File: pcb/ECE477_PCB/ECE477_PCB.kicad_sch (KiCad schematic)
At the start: 88 parts, among them J1 DEBUG, J10 ToF 5, J11 Pi Zero, J2 USB_B_Micro, J3 ESC, J4 ELRS, J5 AUX_PWR, J6 ToF 1, J7 ToF 2, J8 ToF 3, J9 ToF 4, M1 Brushed_DC, M2 Brushed_DC, M3 Brushed_DC, M4 Brushed_DC, Q1 IRLML6244TR, Q2 IRLML6244TR, Q3 IRLML6244TR, Q4 IRLML6244TR, SW1 RESET, U1 STM32F446RETx, U2 Pololu_S13V10F5, U3 REG1117-3.3, U4 FT230XQ, Y1 16MHz X322516MLB4SI

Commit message: completed first rev of PCB. looks like the Pi connector needs moved slightly, board radius is off but drill positions are still the same
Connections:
- net SPI1_CS: now reaches U1.20 (PA4)
- net SPI1_CS2: now reaches U1.24 (PC4)
- no-connect marks 32 -> 31
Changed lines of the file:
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@@
   (no_connect (at 193.04 38.1))
   (no_connect (at 245.11 83.82))
-  (no_connect (at 208.28 132.08))
   (no_connect (at 208.28 121.92))
   (no_connect (at 208.28 116.84))
@@
     (stroke (width 0) (type default) (color 0 0 0 0))
   )
+  (wire (pts (xy 243.84 91.44) (xy 245.11 91.44))
+    (stroke (width 0) (type default) (color 0 0 0 0))
+  )
   (wire (pts (xy 170.18 106.68) (xy 175.26 106.68))
     (stroke (width 0) (type default) (color 0 0 0 0))
@@
     (stroke (width 0) (type default) (color 0 0 0 0))
   )
+  (wire (pts (xy 205.105 132.08) (xy 208.28 132.08))
+    (stroke (width 0) (type default) (color 0 0 0 0))
+  )
   (wire (pts (xy 234.95 59.69) (xy 234.95 60.96))
     (stroke (width 0) (type default) (color 0 0 0 0))
@@
     )
   )
+  (global_label "SPI1_CS2" (shape input) (at 205.105 132.08 180) (fields_autoplaced)
+    (effects (font (size 1.27 1.27)) (justify right))
+    (property "Intersheet References" "${INTERSHEET_REFS}" (id 0) (at 193.8303 132.0006 0)
+      (effects (font (size 1.27 1.27)) (justify right) hide)
+    )
+  )
   (global_label "SPI2_MOSI" (shape input) (at 207.01 124.46 180) (fields_autoplaced)
     (effects (font (size 1.27 1.27)) (justify right))
@@
     )
   )
+  (global_label "SPI1_CS" (shape input) (at 245.11 91.44 0) (fields_autoplaced)
+    (effects (font (size 1.27 1.27)) (justify left))
+    (property "Intersheet References" "${INTERSHEET_REFS}" (id 0) (at 255.1752 91.3606 0)
+      (effects (font (size 1.27 1.27)) (justify left) hide)
+    )
+  )
   (global_label "SYS_JTCL-SWCLK" (shape input) (at 237.49 24.13 180) (fields_autoplaced)
     (effects (font (size 1.27 1.27)) (justify right))
@@
       (reference "#PWR056") (unit 1) (value "GND") (footprint "")
     )
-    (path "/00000000-0000-0000-0000-0000638ac442/00000000-0000-0000-0000-0000638b6240"
+    (path "/00000000-0000-0000-0000-0000638ac442/d259a370-9207-4427-a711-3b1841ea3bc7"
       (reference "#PWR057") (unit 1) (value "+3.3V") (footprint "")
     )
-    (path "/00000000-0000-0000-0000-0000638ac442/00000000-0000-0000-0000-0000638b6236"
-      (reference "#PWR058") (unit 1) (value "GND") (footprint "")
+    (path "/00000000-0000-0000-0000-0000638ac442/873bb88c-fb76-4c4a-925e-44af94ab9263"
+      (reference "#PWR058") (unit 1) (value "+3.3V") (footprint "")
     )
-    (path "/00000000-0000-0000-0000-0000638ac442/00000000-0000-0000-0000-0000638b6252"
+    (path "/00000000-0000-0000-0000-0000638ac442/374d48d2-737f-49f5-b686-017a25b9d0cf"
       (reference "#PWR059") (unit 1) (value "GND") (footprint "")
     )
-    (path "/00000000-0000-0000-0000-0000638ac442/00000000-0000-0000-0000-0000638b6271"
+    (path "/00000000-0000-0000-0000-0000638ac442/4f01b777-ab3f-440b-8300-2f8298ec9b11"
       (reference "#PWR060") (unit 1) (value "+3.3V") (footprint "")
     )
-    (path "/00000000-0000-0000-0000-0000638ac442/00000000-0000-0000-0000-0000638b6277"
-      (reference "#PWR061") (unit 1) (value "+3.3V") (footprint "")
+    (path "/00000000-0000-0000-0000-0000638ac442/bcd24a3e-5c1a-4499-b74a-30a3abea8c8c"
+      (reference "#PWR061") (unit 1) (value "GND") (footprint "")
     )
-    (path "/00000000-0000-0000-0000-0000638ac442/00000000-0000-0000-0000-0000638b6287"
+    (path "/00000000-0000-0000-0000-0000638ac442/3696a052-0d1e-470f-a6eb-e4b59c87443d"
       (reference "#PWR062") (unit 1) (value "GND") (footprint "")
     )
-    (path "/00000000-0000-0000-0000-0000638ac442/00000000-0000-0000-0000-0000638b621a"
+    (path "/00000000-0000-0000-0000-0000638ac442/14ff9f61-be56-4292-8845-23321af0ae8d"
       (reference "#PWR063") (unit 1) (value "GND") (footprint "")
     )
-    (path "/00000000-0000-0000-0000-0000638ac442/00000000-0000-0000-0000-0000638b6220"
+    (path "/00000000-0000-0000-0000-0000638ac442/b9c9ecf9-e9c1-4e6f-aecc-250db8ad1b17"
       (reference "#PWR064") (unit 1) (value "GND") (footprint "")
     )
-    (path "/00000000-0000-0000-0000-0000638ac442/00000000-0000-0000-0000-0000638b6281"
+    (path "/00000000-0000-0000-0000-0000638ac442/c7525157-945c-4967-8e97-f7126c8df6bb"
       (reference "#PWR065") (unit 1) (value "GND") (footprint "")
     )
@@
       (reference "#PWR0103") (unit 1) (value "GND") (footprint "")
     )
+    (path "/00000000-0000-0000-0000-0000638ac442/1c9c31c6-bd07-4756-9670-24da259f533e"
+      (reference "#PWR0104") (unit 1) (value "GND") (footprint "")
+    )
     (path "/00000000-0000-0000-0000-00005d183881"
       (reference "C1") (unit 1) (value "100uF") (footprint "Capacitor_SMD:C_Elec_3x5.4")
@@
       (reference "C24") (unit 1) (value "0.1uF") (footprint "Capacitor_SMD:C_0402_1005Metric")
     )
-    (path "/00000000-0000-0000-0000-0000638ac442/00000000-0000-0000-0000-0000638b6230"
-      (reference "C25") (unit 1) (value "10nF, 4V") (footprint "Capacitor_SMD:C_0402_1005Metric")
+    (path "/00000000-0000-0000-0000-0000638ac442/72f59762-bf8b-4064-8dc0-e11f9dcd9524"
+      (reference "C25") (unit 1) (value "0.1uF 4V") (footprint "Capacitor_SMD:C_0603_1608Metric")
     )
     (path "/00000000-0000-0000-0000-0000638ac442/00000000-0000-0000-0000-0000638b624c"
-      (reference "C26") (unit 1) (value "0.1uF 4V") (footprint "Capacitor_SMD:C_0402_1005Metric")
-    )
-    (path "/00000000-0000-0000-0000-0000638ac442/00000000-0000-0000-0000-0000638b6214"
-      (reference "C27") (unit 1) (value "0.1uF 2V") (footprint "Capacitor_SMD:C_0402_1005Metric")
+      (reference "C26") (unit 1) (value "0.1uF 4V") (footprint "Capacitor_SMD:C_0603_1608Metric")
     )
-    (path "/00000000-0000-0000-0000-0000638ac442/00000000-0000-0000-0000-0000638b620c"
-      (reference "C28") (unit 1) (value "2.2nF, 50V") (footprint "Capacitor_SMD:C_0603_1608Metric")
+    (path "/00000000-0000-0000-0000-0000638ac442/1ed0f3c2-3fec-4eb5-a50f-c84878be7e1e"
+      (reference "C27") (unit 1) (value "0.1uF 4V") (footprint "Capacitor_SMD:C_0603_1608Metric")
     )
     (path "/0312643c-df93-4304-9858-72b871182e4e"
@@
     )
     (path "/00000000-0000-0000-0000-0000638ac442/00000000-0000-0000-0000-0000638b625f"
-      (reference "R22") (unit 1) (value "4.7K") (footprint "Resistor_SMD:R_0603_1608Metric")
+      (reference "R22") (unit 1) (value "0") (footprint "Resistor_SMD:R_0603_1608Metric")
     )
     (path "/00000000-0000-0000-0000-0000638ac442/00000000-0000-0000-0000-0000638b6267"
-      (reference "R23") (unit 1) (value "4.7K") (footprint "Resistor_SMD:R_0603_1608Metric")
+      (reference "R23") (unit 1) (value "0") (footprint "Resistor_SMD:R_0603_1608Metric")
     )
     (path "/37df3ae6-4c60-47ed-8958-65dd81c8fddc"
@@
       (reference "R25") (unit 1) (value "4.7K") (footprint "Resistor_SMD:R_0603_1608Metric")
     )
+    (path "/00000000-0000-0000-0000-0000638ac442/7503b914-d557-4a20-9922-b4e36a0d43b0"
+      (reference "R26") (unit 1) (value "4.7k") (footprint "Resistor_SMD:R_0603_1608Metric")
+    )
+    (path "/00000000-0000-0000-0000-0000638ac442/393fa92e-1b94-4287-a0ad-690389282aae"
+      (reference "R27") (unit 1) (value "4.7k") (footprint "Resistor_SMD:R_0603_1608Metric")
+    )
+    (path "/00000000-0000-0000-0000-0000638ac442/796501ad-8a25-4132-a38f-866f10c4021c"
+      (reference "R28") (unit 1) (value "0") (footprint "Resistor_SMD:R_0603_1608Metric")
+    )
+    (path "/00000000-0000-0000-0000-0000638ac442/33a1f482-0b6e-4f0a-b75a-bf5bb719e12a"
+      (reference "R29") (unit 1) (value "0") (footprint "Resistor_SMD:R_0603_1608Metric")
+    )
     (path "/00000000-0000-0000-0000-00005d1f1728"

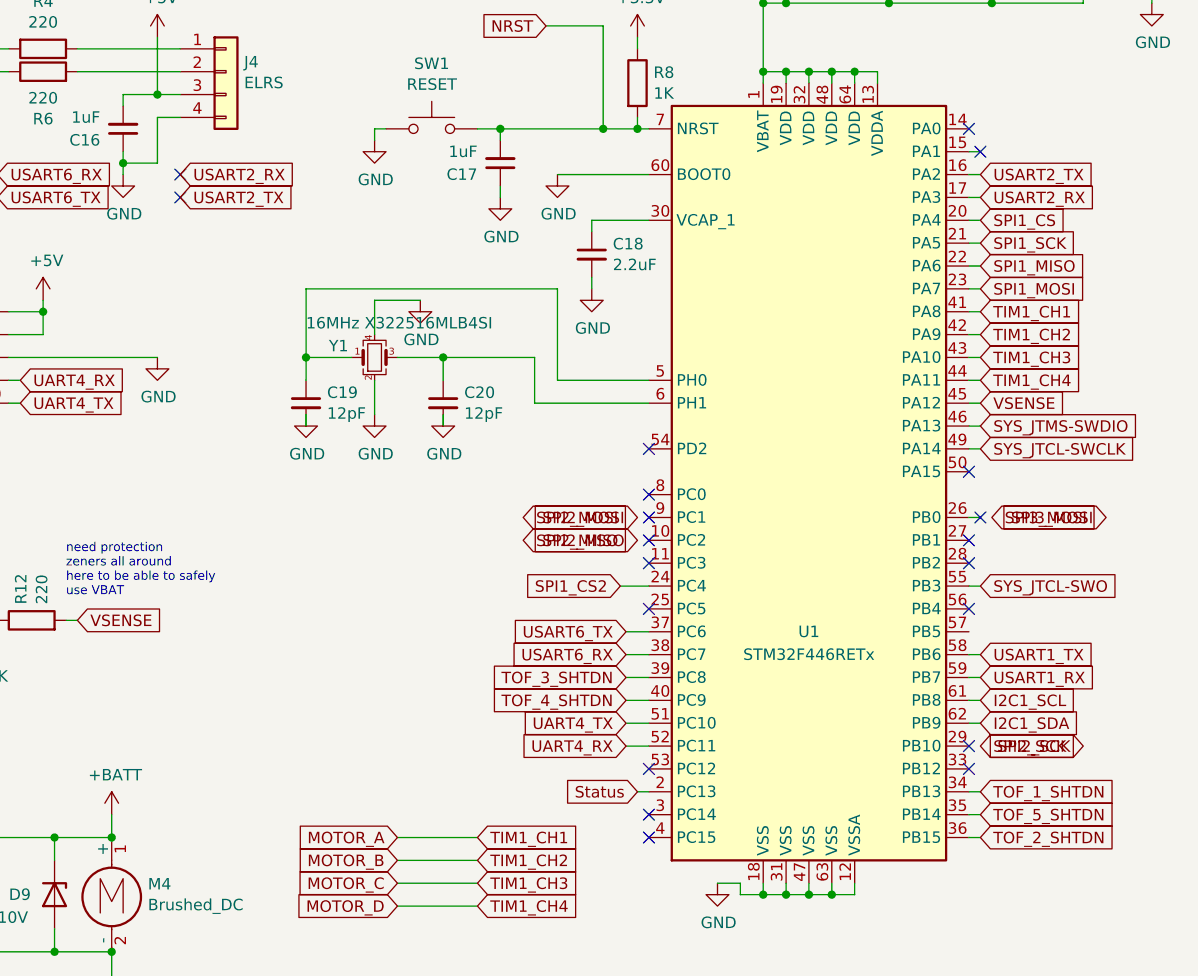
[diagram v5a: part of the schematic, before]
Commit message: fixed vias, added test points, fixed ground plane in some spots
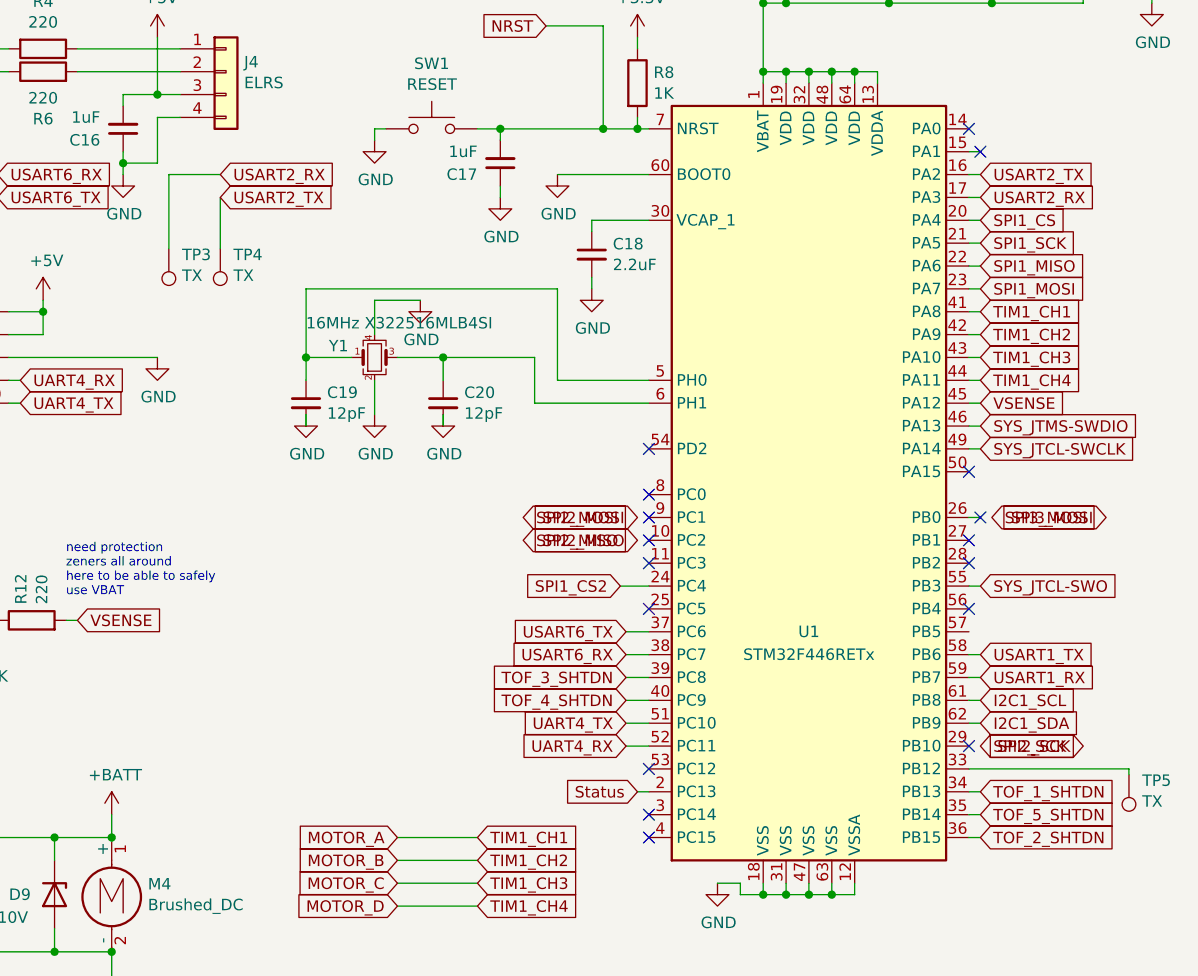
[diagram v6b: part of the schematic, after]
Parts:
- added TP3, TP4, TP5: TX, TestPoint:TestPoint_Pad_D1.0mm, symbol Connector:TestPoint
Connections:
- net USART2_RX: now also TP3.1
- net USART2_TX: now also TP4.1
- net at U1.33 (PB12): now also TP5.1
- no-connect marks 31 -> 28
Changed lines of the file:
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@@
   (no_connect (at 124.46 106.68))
   (no_connect (at 124.46 109.22))
-  (no_connect (at 156.21 86.36))
-  (no_connect (at 156.21 88.9))
   (no_connect (at 193.04 35.56))
   (no_connect (at 208.28 160.02))
@@
   (no_connect (at 208.28 121.92))
   (no_connect (at 208.28 116.84))
-  (no_connect (at 243.84 152.4))
   (no_connect (at 208.28 134.62))
   (no_connect (at 238.76 29.21))
@@
     (stroke (width 0) (type default) (color 0 0 0 0))
   )
+  (wire (pts (xy 160.655 88.9) (xy 160.655 94.615))
+    (stroke (width 0) (type default) (color 0 0 0 0))
+  )
   (wire (pts (xy 34.29 160.02) (xy 34.29 157.48))
     (stroke (width 0) (type default) (color 0 0 0 0))
@@
     (stroke (width 0) (type default) (color 0 0 0 0))
   )
+  (wire (pts (xy 261.62 153.035) (xy 261.62 152.4))
+    (stroke (width 0) (type default) (color 0 0 0 0))
+  )
   (wire (pts (xy 22.86 63.5) (xy 22.86 62.23))
     (stroke (width 0) (type default) (color 0 0 0 0))
@@
     (stroke (width 0) (type default) (color 0 0 0 0))
   )
+  (wire (pts (xy 154.94 94.615) (xy 154.94 86.36))
+    (stroke (width 0) (type default) (color 0 0 0 0))
+  )
   (wire (pts (xy 30.48 80.01) (xy 30.48 78.74))
     (stroke (width 0) (type default) (color 0 0 0 0))
@@
     (stroke (width 0) (type default) (color 0 0 0 0))
   )
+  (wire (pts (xy 154.94 86.36) (xy 160.655 86.36))
+    (stroke (width 0) (type default) (color 0 0 0 0))
+  )
   (wire (pts (xy 134.62 88.9) (xy 135.89 88.9))
     (stroke (width 0) (type default) (color 0 0 0 0))
   )
+  (wire (pts (xy 243.84 152.4) (xy 261.62 152.4))
+    (stroke (width 0) (type default) (color 0 0 0 0))
+  )
   (wire (pts (xy 31.75 135.89) (xy 29.21 135.89))
     (stroke (width 0) (type default) (color 0 0 0 0))
@@
     )
   )
-  (global_label "USART2_RX" (shape input) (at 156.21 86.36 0) (fields_autoplaced)
+  (global_label "USART2_RX" (shape input) (at 160.655 86.36 0) (fields_autoplaced)
     (effects (font (size 1.27 1.27)) (justify left))
-    (property "Intersheet References" "${INTERSHEET_REFS}" (id 0) (at 169.0571 86.2806 0)
+    (property "Intersheet References" "${INTERSHEET_REFS}" (id 0) (at 173.5021 86.2806 0)
       (effects (font (size 1.27 1.27)) (justify left) hide)
     )
@@
     )
   )
-  (global_label "USART2_TX" (shape input) (at 156.21 88.9 0) (fields_autoplaced)
+  (global_label "USART2_TX" (shape input) (at 160.655 88.9 0) (fields_autoplaced)
     (effects (font (size 1.27 1.27)) (justify left))
-    (property "Intersheet References" "${INTERSHEET_REFS}" (id 0) (at 168.7547 88.8206 0)
+    (property "Intersheet References" "${INTERSHEET_REFS}" (id 0) (at 173.1997 88.8206 0)
       (effects (font (size 1.27 1.27)) (justify left) hide)
     )
@@
     (pin "1")
     (pin "10")
-    (pin "MP")
     (pin "2")
     (pin "3")
@@
     (pin "8")
     (pin "9")
+    (pin "MP")
   )
   (symbol (lib_id "power:GND") (at 25.4 36.83 90) (unit 1)
@@
     (pin "2")
   )
+  (symbol (lib_id "Connector:TestPoint") (at 261.62 153.035 180) (unit 1)
+    (in_bom yes) (on_board yes)
+    (property "Reference" "TP5" (id 0) (at 263.0932 153.6954 0)
+      (effects (font (size 1.27 1.27)) (justify right))
+    )
+    (property "Value" "TX" (id 1) (at 263.0932 156.0068 0)
+      (effects (font (size 1.27 1.27)) (justify right))
+    )
+    (property "Footprint" "TestPoint:TestPoint_Pad_D1.0mm" (id 2) (at 256.54 153.035 0)
+      (effects (font (size 1.27 1.27)) hide)
+    )
+    (property "Datasheet" "~" (id 3) (at 256.54 153.035 0)
+      (effects (font (size 1.27 1.27)) hide)
+    )
+    (pin "1")
+  )
   (symbol (lib_id "Mechanical:MountingHole") (at 111.76 83.82 0) (unit 1)
     (in_bom yes) (on_board yes) (fields_autoplaced)
@@
     (pin "2")
   )
+  (symbol (lib_id "Connector:TestPoint") (at 160.655 94.615 180) (unit 1)
+    (in_bom yes) (on_board yes)
+    (property "Reference" "TP4" (id 0) (at 162.1282 95.2754 0)
+      (effects (font (size 1.27 1.27)) (justify right))
+    )
+    (property "Value" "TX" (id 1) (at 162.1282 97.5868 0)
+      (effects (font (size 1.27 1.27)) (justify right))
+    )
+    (property "Footprint" "TestPoint:TestPoint_Pad_D1.0mm" (id 2) (at 155.575 94.615 0)
+      (effects (font (size 1.27 1.27)) hide)
+    )
+    (property "Datasheet" "~" (id 3) (at 155.575 94.615 0)
+      (effects (font (size 1.27 1.27)) hide)
+    )
+    (pin "1")
+  )
   (symbol (lib_id "power:GND") (at 153.67 106.68 0) (unit 1)
     (in_bom yes) (on_board yes)
@@
     (pin "1")
   )
+  (symbol (lib_id "Connector:TestPoint") (at 154.94 94.615 180) (unit 1)
+    (in_bom yes) (on_board yes)
+    (property "Reference" "TP3" (id 0) (at 156.4132 95.2754 0)
+      (effects (font (size 1.27 1.27)) (justify right))
+    )
+    (property "Value" "TX" (id 1) (at 156.4132 97.5868 0)
+      (effects (font (size 1.27 1.27)) (justify right))
+    )
+    (property "Footprint" "TestPoint:TestPoint_Pad_D1.0mm" (id 2) (at 149.86 94.615 0)
+      (effects (font (size 1.27 1.27)) hide)
+    )
+    (property "Datasheet" "~" (id 3) (at 149.86 94.615 0)
+      (effects (font (size 1.27 1.27)) hide)
+    )
+    (pin "1")
+  )
   (symbol (lib_id "power:GND") (at 97.79 87.63 0) (unit 1)
     (in_bom yes) (on_board yes)
@@
       (reference "TP2") (unit 1) (value "CRT") (footprint "TestPoint:TestPoint_Pad_D1.0mm")
     )
+    (path "/bf65c22a-dab3-4d42-9b19-be4be34d005f"
+      (reference "TP3") (unit 1) (value "TX") (footprint "TestPoint:TestPoint_Pad_D1.0mm")
+    )
+    (path "/a877a6ae-af0d-43ad-ba07-97a9b363c4ed"
+      (reference "TP4") (unit 1) (value "TX") (footprint "TestPoint:TestPoint_Pad_D1.0mm")
+    )
+    (path "/4ec5e413-260f-443e-a906-7f6522938357"
+      (reference "TP5") (unit 1) (value "TX") (footprint "TestPoint:TestPoint_Pad_D1.0mm")
+    )
     (path "/00000000-0000-0000-0000-00005d1d966a"

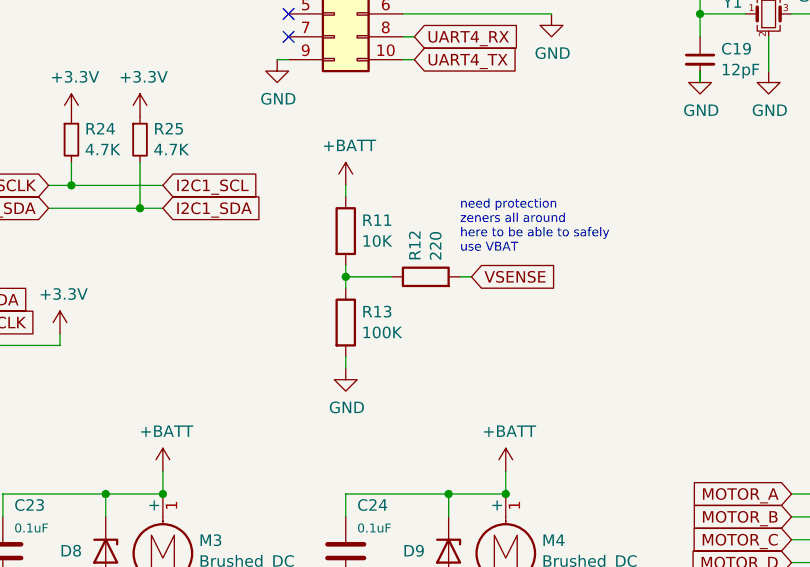
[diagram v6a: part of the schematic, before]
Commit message: fixed resistor divider and added keepout under the oscillator
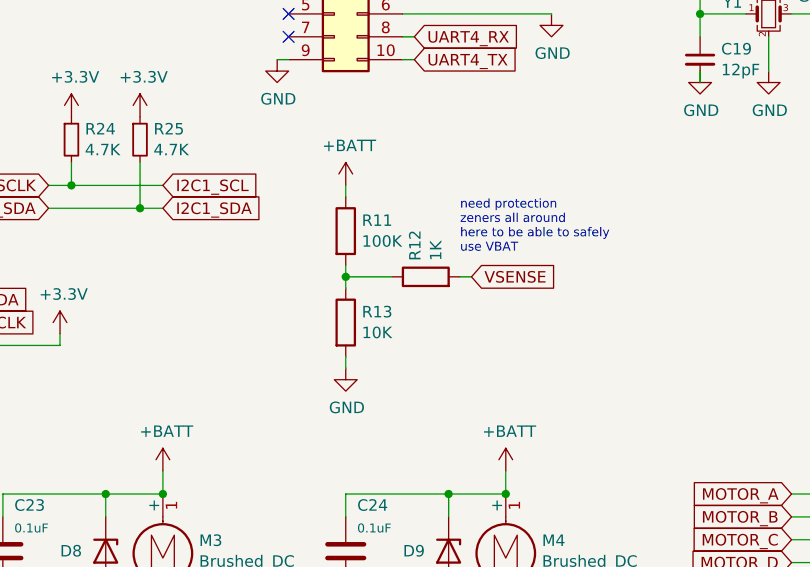
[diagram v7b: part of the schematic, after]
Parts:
- R11: value 10K -> 100K
- R12: value 220 -> 1K
- R13: value 100K -> 10K
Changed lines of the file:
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@@
       (effects (font (size 1.27 1.27)) (justify left))
     )
-    (property "Value" "10K" (id 1) (at 132.588 131.953 0)
+    (property "Value" "100K" (id 1) (at 132.588 131.953 0)
       (effects (font (size 1.27 1.27)) (justify left))
     )
@@
       (effects (font (size 1.27 1.27)) (justify left))
     )
-    (property "Value" "100K" (id 1) (at 132.588 142.113 0)
+    (property "Value" "10K" (id 1) (at 132.588 142.113 0)
       (effects (font (size 1.27 1.27)) (justify left))
     )
@@
       (effects (font (size 1.27 1.27)) (justify left))
     )
-    (property "Value" "220" (id 1) (at 140.843 134.112 0)
+    (property "Value" "1K" (id 1) (at 140.843 134.112 0)
       (effects (font (size 1.27 1.27)) (justify left))
     )
@@
     )
     (path "/00000000-0000-0000-0000-00005ea7f42d"
-      (reference "R11") (unit 1) (value "10K") (footprint "Resistor_SMD:R_0603_1608Metric")
+      (reference "R11") (unit 1) (value "100K") (footprint "Resistor_SMD:R_0603_1608Metric")
     )
     (path "/00000000-0000-0000-0000-0000635e4af8"
-      (reference "R12") (unit 1) (value "220") (footprint "Resistor_SMD:R_0603_1608Metric")
+      (reference "R12") (unit 1) (value "1K") (footprint "Resistor_SMD:R_0603_1608Metric")
     )
     (path "/00000000-0000-0000-0000-00005ea7f4c7"
-      (reference "R13") (unit 1) (value "100K") (footprint "Resistor_SMD:R_0603_1608Metric")
+      (reference "R13") (unit 1) (value "10K") (footprint "Resistor_SMD:R_0603_1608Metric")
     )
     (path "/00000000-0000-0000-0000-00005d1e662b"
